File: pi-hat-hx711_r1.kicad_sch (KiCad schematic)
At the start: 19 parts, among them J1 GPIO, J2 Conn_01x06, J3 Conn_01x06, J4 Conn_01x06, J5 Conn_01x06, J6 Conn_01x04, U1 M24c64, U3 XC6206P332MR

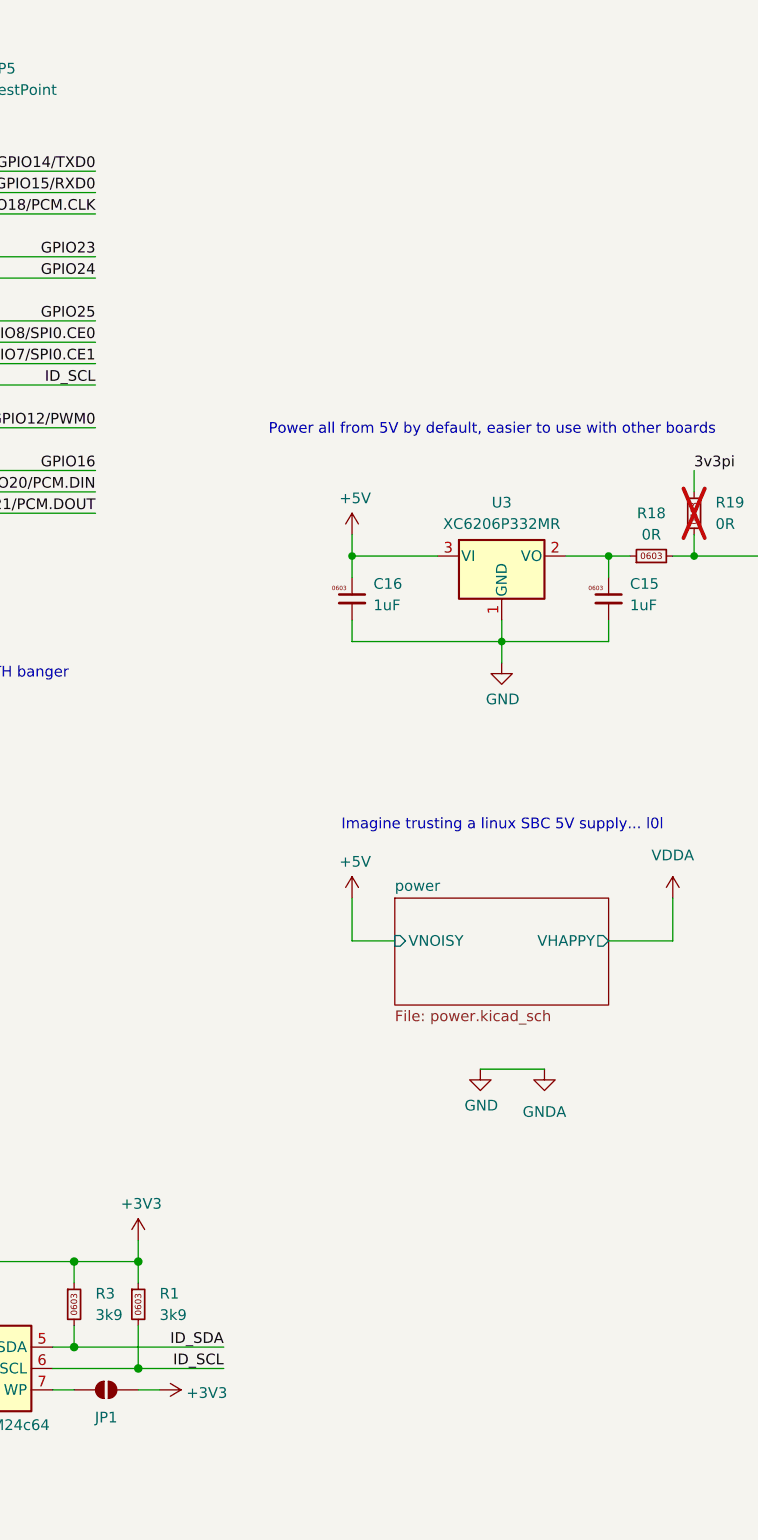
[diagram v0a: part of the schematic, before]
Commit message: adds a 2 pin power in connector
I don't have any suitable power supplies for RPi, so just put on a
connector to use external if desired.  Totally raw unprotected, just
feeds straight to the rpi.
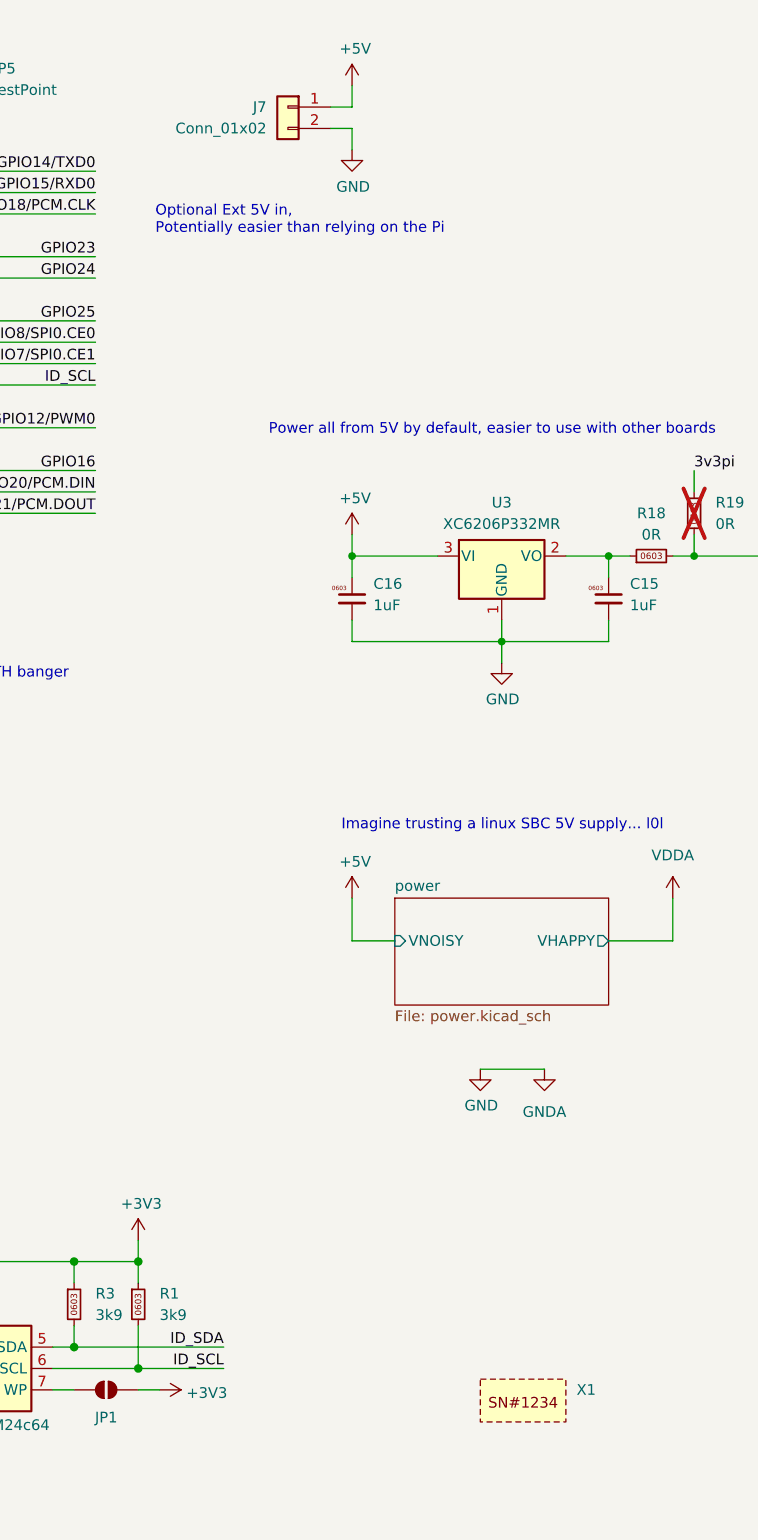
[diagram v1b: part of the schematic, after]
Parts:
- added J7: Conn_01x02, Connector_Phoenix_MC:PhoenixContact_MCV_1,5_2-G-3.81_1x02_P3.81mm_Vertical, symbol Connector_Generic:Conn_01x02
- added X1: ~, jlc-extras:JLC_2D_BARCODE_8x8mm, symbol karl-marel-atomics:SYM_LABEL
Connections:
- net +5V: now also J7.1 (Pin_1)
- net GND: now also J7.2 (Pin_2)
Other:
- note added: "Optional Ext 5V in, Potentially easier than relying on the Pi"
